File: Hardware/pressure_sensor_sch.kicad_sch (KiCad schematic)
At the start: 40 parts, among them IC5 ADS131M04IRUKR, J4 1053131104, J5 1053131104, J6 1053131104, J7 1053131104

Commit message: wrapping up layout
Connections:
- net +3.3V is gone; now on net +3V3: IC5.9 (~{SYNC}/~{RESET})
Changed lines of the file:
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@@
 	(wire
 		(pts
+			(xy 112.776 105.156) (xy 112.776 107.95)
+		)
+		(stroke
+			(width 0)
+			(type default)
+		)
+	)
+	(wire
+		(pts
 			(xy 169.418 105.156) (xy 156.464 105.156)
 		)
@@
 	(wire
 		(pts
-			(xy 100.33 107.95) (xy 105.41 107.95)
+			(xy 100.33 107.95) (xy 112.776 107.95)
 		)
 		(stroke
@@
 	)
 	(symbol
-		(lib_name "+3.3V_1")
-		(lib_id "power:+3.3V")
-		(at 105.41 107.95 270)
+		(lib_id "power:+3V3")
+		(at 112.776 105.156 0)
 		(unit 1)
 		(exclude_from_sim no)
@@
 		(on_board yes)
 		(dnp no)
-		(property "Reference" "#PWR092"
-			(at 101.6 107.95 0)
+		(fields_autoplaced yes)
+		(property "Reference" "#PWR015"
+			(at 112.776 108.966 0)
 			(effects
 				(font
@@
 			)
 		)
-		(property "Value" "+3.3V"
-			(at 109.22 109.22 0)
+		(property "Value" "+3V3"
+			(at 112.776 101.0229 0)
 			(effects
 				(font
@@
 		)
 		(property "Footprint" ""
-			(at 105.41 107.95 0)
+			(at 112.776 105.156 0)
 			(effects
 				(font
@@
 		)
 		(property "Datasheet" ""
-			(at 105.41 107.95 0)
+			(at 112.776 105.156 0)
 			(effects
 				(font
@@
 			)
 		)
-		(property "Description" ""
-			(at 105.41 107.95 0)
+		(property "Description" "Power symbol creates a global label with name \"+3V3\""
+			(at 112.776 105.156 0)
 			(effects
 				(font
@@
 			(project "Ricardo-Kermit-Mini"
 				(path "/7db990e4-92e1-4f99-b4d2-435bbec1ba83/69b1b5a9-b31d-4274-9c5e-37e99dc58839"
-					(reference "#PWR092")
+					(reference "#PWR015")
 					(unit 1)
 				)

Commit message: layout
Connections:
- net GND: now also IC5.21 (EP)
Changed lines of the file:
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@@
+	)
+	(junction
+		(at 46.736 115.57)
+		(diameter 0)
+		(color 0 0 0 0)
 	)
 	(junction
@@
 	(wire
 		(pts
+			(xy 46.736 115.57) (xy 46.736 118.11)
+		)
+		(stroke
+			(width 0)
+			(type default)
+		)
+	)
+	(wire
+		(pts
 			(xy 174.752 45.974) (xy 187.96 45.974)
 		)
@@
 	(wire
 		(pts
+			(xy 49.53 118.11) (xy 46.736 118.11)
+		)
+		(stroke
+			(width 0)
+			(type default)
+		)
+	)
+	(wire
+		(pts
 			(xy 237.236 59.182) (xy 239.776 59.182)
 		)
@@
 	(wire
 		(pts
+			(xy 46.736 115.57) (xy 49.53 115.57)
+		)
+		(stroke
+			(width 0)
+			(type default)
+		)
+	)
+	(wire
+		(pts
 			(xy 173.228 72.39) (xy 173.228 81.788)
 		)
@@
 	(wire
 		(pts
-			(xy 35.56 115.57) (xy 49.53 115.57)
-		)
-		(stroke
+			(xy 35.56 115.57) (xy 46.736 115.57)
+		)
+		(stroke

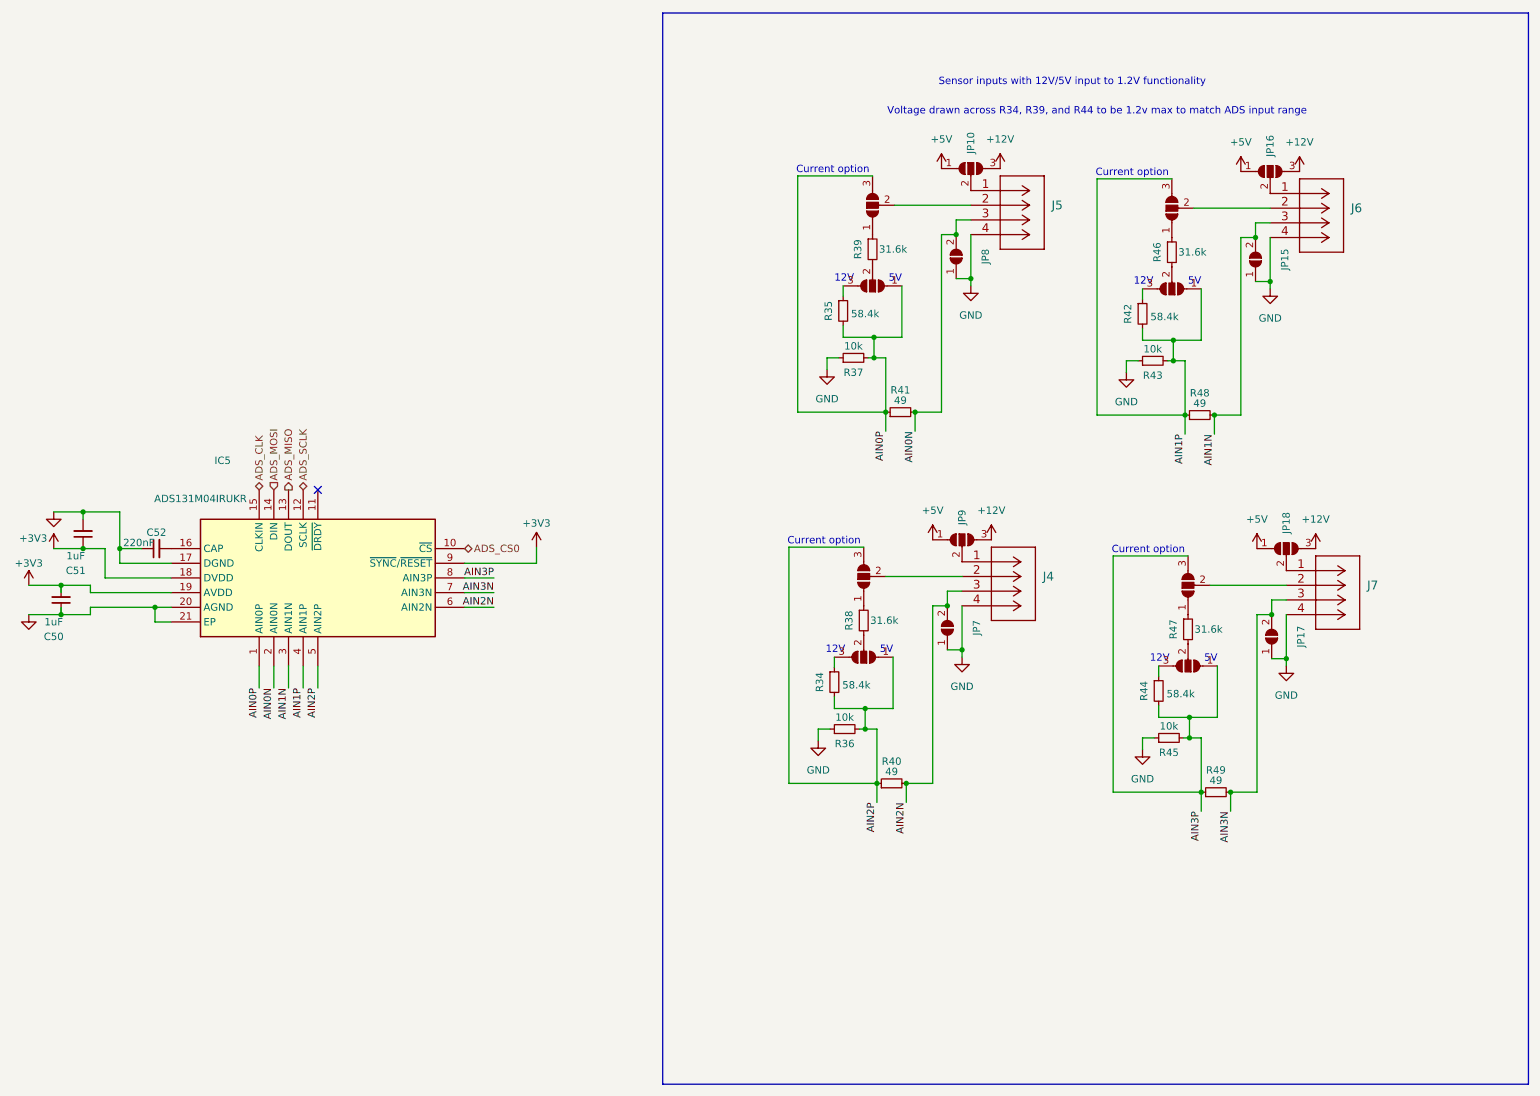
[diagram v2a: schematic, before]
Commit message: added diodes on gpio breakout and sensor supply
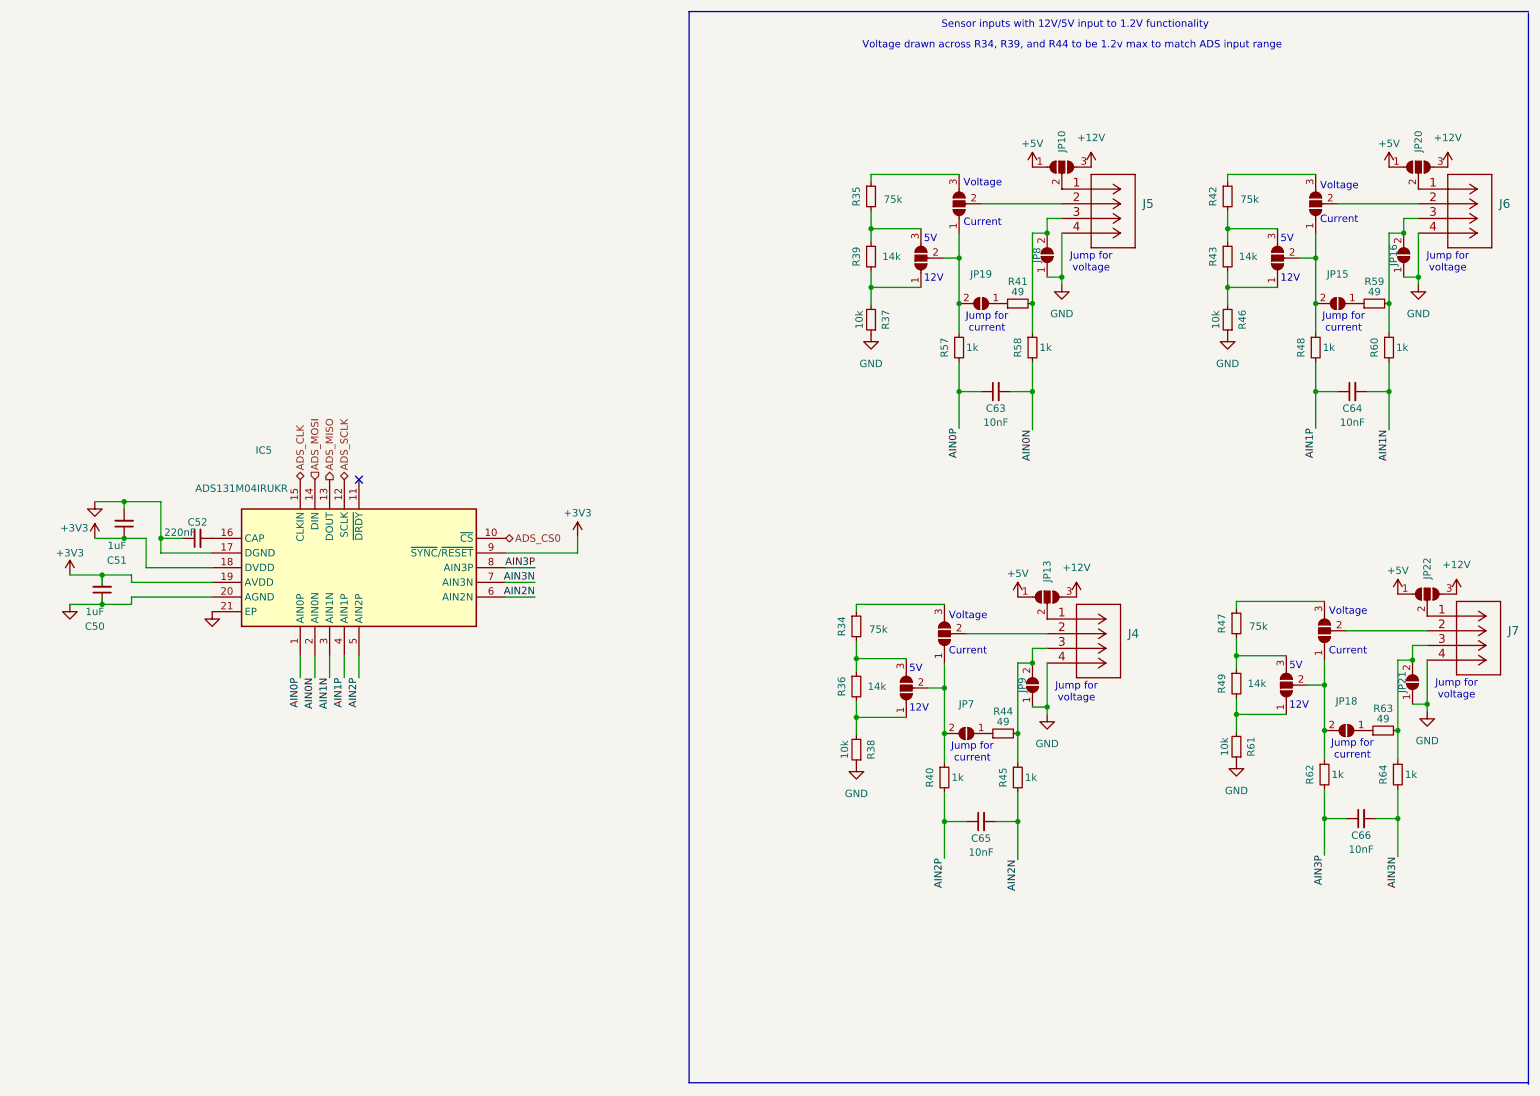
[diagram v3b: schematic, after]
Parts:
- removed JP16, JP18, JP9: SolderJumper_3_Open, Jumper:SolderJumper-3_P1.3mm_Open_RoundedPad1.0x1.5mm_NumberLabels, symbol Jumper:SolderJumper_3_Open
- removed JP17: SolderJumper_2_Open, iclr:SmallerSolderJP, symbol Jumper:SolderJumper_2_Open
- added C63, C64, C65, C66: 10nF, Capacitor_SMD:C_0402_1005Metric, symbol Device:C_Small
- added JP16, JP18, JP19, JP21, JP9: SolderJumper_2_Open, iclr:SmallerSolderJP, symbol Jumper:SolderJumper_2_Open
- added JP17, JP20, JP22: SolderJumper_3_Open, Jumper:SolderJumper-3_P1.3mm_Open_RoundedPad1.0x1.5mm_NumberLabels, symbol Jumper:SolderJumper_3_Open
- added R57, R58, R60, R62, R64: 1k, Resistor_SMD:R_0402_1005Metric, symbol Device:R_Small
- added R59, R63: 49, Resistor_SMD:R_0402_1005Metric, symbol Device:R_Small
- added R61: 10k, Resistor_SMD:R_0402_1005Metric, symbol Device:R_Small
- R34, R35, R42: value 58.4k -> 75k
- R36, R43: value 10k -> 14k
- R38, R46: value 31.6k -> 10k
- R39: value 31.6k -> 14k
- R40, R48: value 49 -> 1k
- R44: value 58.4k -> 49
- R45: value 10k -> 1k
- R47: value 31.6k -> 75k
- R49: value 49 -> 14k
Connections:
- net +12V: now also JP13.3 (B), JP20.3 (B), JP22.3 (B)
- net +5V: now also JP13.1 (A), JP20.1 (A), JP22.1 (A)
- net AIN0N: now also C63.2, R58.2; no longer J5.3, JP8.2 (B), R41.2
- net AIN0P: now also C63.1, R57.2; no longer JP5.3 (B), JP6.1 (A), R35.2, R37.2, R41.1
- net AIN1N: now also C64.2, R60.2; no longer J6.3, JP15.2 (B), R48.2
- net AIN1P: now also R48.2, C64.1; no longer JP11.3 (B), JP12.1 (A), R42.2, R43.2, R48.1
- net AIN2N: now also R45.2, C65.2; no longer J4.3, JP7.2 (B), R40.2
- net AIN2P: now also R40.2, C65.1; no longer JP3.3 (B), JP4.1 (A), R34.2, R36.2, R40.1
- net AIN3N: now also C66.2, R64.2; no longer J7.3, R49.2
- net AIN3P: now also C66.1, R62.2; no longer JP13.3 (B), JP14.1 (A), R44.2, R45.2, R49.1
- net GND: now also R38.1, R46.1, JP16.1 (A), JP21.1 (A), JP9.1 (A), R61.1; no longer JP15.1 (A), JP7.1 (A), R36.1, R43.1, R45.1
- net at JP3.1 (A): now also R36.2, R38.2; no longer R38.1
- net at J4.2: now also JP4.2 (C); no longer JP3.2 (C)
- net at JP11.1 (A): now also R43.2, R46.2; no longer R46.1
- net at JP11.2 (C): now also JP12.1 (A), JP15.2 (B), R48.1; no longer J6.2
- net at JP12.2 (C): now also J6.2; no longer R46.2
- net at R47.1: now also JP17.3 (B); no longer JP13.1 (A)
- net at R47.2: now also JP14.3 (B), R49.1; no longer JP14.2 (C)
- net at R44.1: now also JP7.1 (A); no longer JP14.3 (B)
- net at J6.1: now also JP20.2 (C)
- net at JP6.2 (C): now also JP5.1 (A), JP19.2 (B), R57.1; no longer R39.2
- net at JP6.3 (B): now also R35.2, R39.1; no longer R35.1
- net at J4.1: now also JP13.2 (C)
- net at J7.1: now also JP22.2 (C)
- net at J7.2: now also JP17.2 (C); no longer JP13.2 (C)
- new net: J4.3, JP9.2 (B), R44.2, R45.1
- new net: J5.3, JP8.2 (B), R41.2, R58.1
- new net: JP3.3 (B), R34.2, R36.1
- new net: JP14.1 (A), R49.2, R61.2
- new net: JP15.1 (A), R59.1
- new net: JP19.1 (A), R41.1
- new net: J6.3, JP16.2 (B), R59.2, R60.1
- new net: JP18.1 (A), R63.1
- new net: J7.3, JP21.2 (B), R63.2, R64.1
- new net: JP14.2 (C), JP17.1 (A), JP18.2 (B), R62.1
- new net: JP3.2 (C), JP4.1 (A), JP7.2 (B), R40.1
- new net: JP6.1 (A), R37.2, R39.2
- new net: JP5.3 (B), R35.1
- new net: JP11.3 (B), R42.2, R43.1
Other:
- note added: "Current"
- note added: "Jump for current"
- note added: "Jump for voltage"
- note added: "Voltage"
- note removed: "Current option"
- moved on the sheet: C50, C51, C52, IC5, J5, JP10, JP8, R35, R37, R39, R41

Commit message: update
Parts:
- IC5: MPN (none) -> ADS131M04IRUKR
- R35: MPN (none) -> RT0402BRD0775KL
- R37: MPN (none) -> ERA2ARB103X
- R39: MPN (none) -> 0402WGF1402TCE
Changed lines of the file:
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@@
 	(wire
 		(pts
-			(xy 37.592 113.792) (xy 37.592 115.062)
-		)
-		(stroke
-			(width 0)
-			(type default)
-		)
-	)
-	(wire
-		(pts
 			(xy 247.65 62.992) (xy 247.65 68.072)
 		)
@@
 	(wire
 		(pts
-			(xy 37.592 109.982) (xy 37.592 111.252)
-		)
-		(stroke
-			(width 0)
-			(type default)
-		)
-	)
-	(wire
-		(pts
 			(xy 198.628 78.232) (xy 198.628 73.152)
 		)
@@
 			)
 		)
+		(property "MPN" "ADS131M04IRUKR"
+			(at 71.882 123.952 90)
+			(effects
+				(font
+					(size 1.27 1.27)
+				)
+				(hide yes)
+			)
+		)
 		(pin "11"
 		)
@@
 			)
 		)
+		(property "MPN" "RT0402BRD0775KL"
+			(at 170.688 44.45 90)
+			(effects
+				(font
+					(size 1.27 1.27)
+				)
+				(hide yes)
+			)
+		)
 		(pin "1"
 		)
@@
 			)
 		)
+		(property "MPN" "0402WGF1402TCE"
+			(at 170.688 54.864 90)
+			(effects
+				(font
+					(size 1.27 1.27)
+				)
+				(hide yes)
+			)
+		)
 		(pin "1"
 		)
@@
 			(effects
 				(font
+					(size 1.27 1.27)
+				)
+				(hide yes)
+			)
+		)
+		(property "MPN" " ERA2ARB103X"
+			(at 170.688 65.786 90)
+			(effects
+				(font

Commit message: changes post 3rd review
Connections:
- net ADS_DRDY: now reaches IC5.11 (~{DRDY})
- no-connect marks 1 -> 0
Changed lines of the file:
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@@
 		(color 0 0 0 0)
-	)
-	(no_connect
-		(at 82.042 93.472)
 	)
 	(wire
@@
 		(fields_autoplaced yes)
 		(effects
+			(font
+				(size 1.27 1.27)
+			)
+			(justify left)
+		)
+	)
+	(hierarchical_label "ADS_DRDY"
+		(shape output)
+		(at 82.042 93.472 90)
+		(fields_autoplaced yes)
+		(effects

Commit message: post Andrei review, new SD
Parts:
- R41, R44, R59, R63: value 49 -> 49.9; MPN (none) -> RT0402BRD0749R9L
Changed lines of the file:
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@@
 		)
 	)
-	(text "Jump for \nvoltage"
-		(exclude_from_sim no)
-		(at 272.034 131.572 0)
-		(effects
-			(font
-				(size 1.27 1.27)
-			)
-			(justify bottom)
-		)
-	)
 	(text "Current"
 		(exclude_from_sim no)
@@
 			)
 		)
-		(property "Value" "49"
+		(property "Value" "49.9"
 			(at 259.334 134.874 90)
 			(effects
@@
 			)
 		)
+		(property "MPN" "RT0402BRD0749R9L"
+			(at 259.334 136.906 90)
+			(effects
+				(font
+					(size 1.27 1.27)
+				)
+				(hide yes)
+			)
+		)
 		(pin "1"
 		)
@@
 			)
 		)
-		(property "Value" "49"
+		(property "Value" "49.9"
 			(at 193.548 135.382 90)
 			(effects
@@
 			)
 		)
+		(property "MPN" "RT0402BRD0749R9L"
+			(at 193.548 137.414 90)
+			(effects
+				(font
+					(size 1.27 1.27)
+				)
+				(hide yes)
+			)
+		)
 		(pin "1"
 		)
@@
 			)
 		)
-		(property "Value" "49"
+		(property "Value" "49.9"
 			(at 257.81 60.96 90)
 			(effects
@@
 			)
 		)
+		(property "MPN" "RT0402BRD0749R9L"
+			(at 257.81 62.992 90)
+			(effects
+				(font
+					(size 1.27 1.27)
+				)
+				(hide yes)
+			)
+		)
 		(pin "1"
 		)
@@
 			)
 		)
-		(property "Value" "49"
+		(property "Value" "49.9"
 			(at 196.088 60.96 90)
 			(effects
@@
 			(effects
 				(font
+					(size 1.27 1.27)
+				)
+				(hide yes)
+			)
+		)
+		(property "MPN" "RT0402BRD0749R9L"
+			(at 196.088 62.992 90)
+			(effects
+				(font
